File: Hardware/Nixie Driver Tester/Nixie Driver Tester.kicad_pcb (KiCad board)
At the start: 2 copper layers, 46.4 x 45.1 mm, 33 parts, among them J1 ICSP, J2 UJC-HP-3-SMT-TR, J3 OLED, Q1 MMBT2222A, Q2 MMBT2907ALT1G, Q3 FDD7N25LZTM, SW1 SW_Omron_B3FS

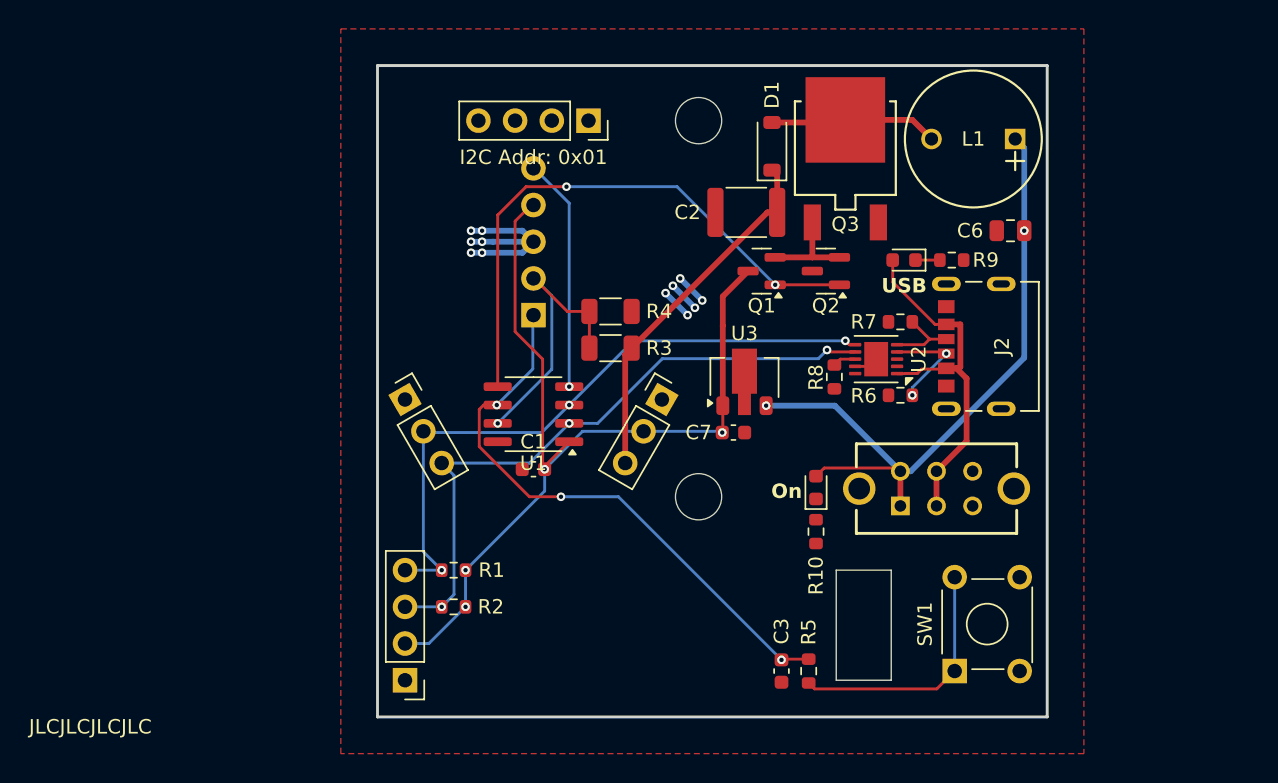
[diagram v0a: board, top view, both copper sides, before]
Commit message: Using a STM32 instead of a PIC
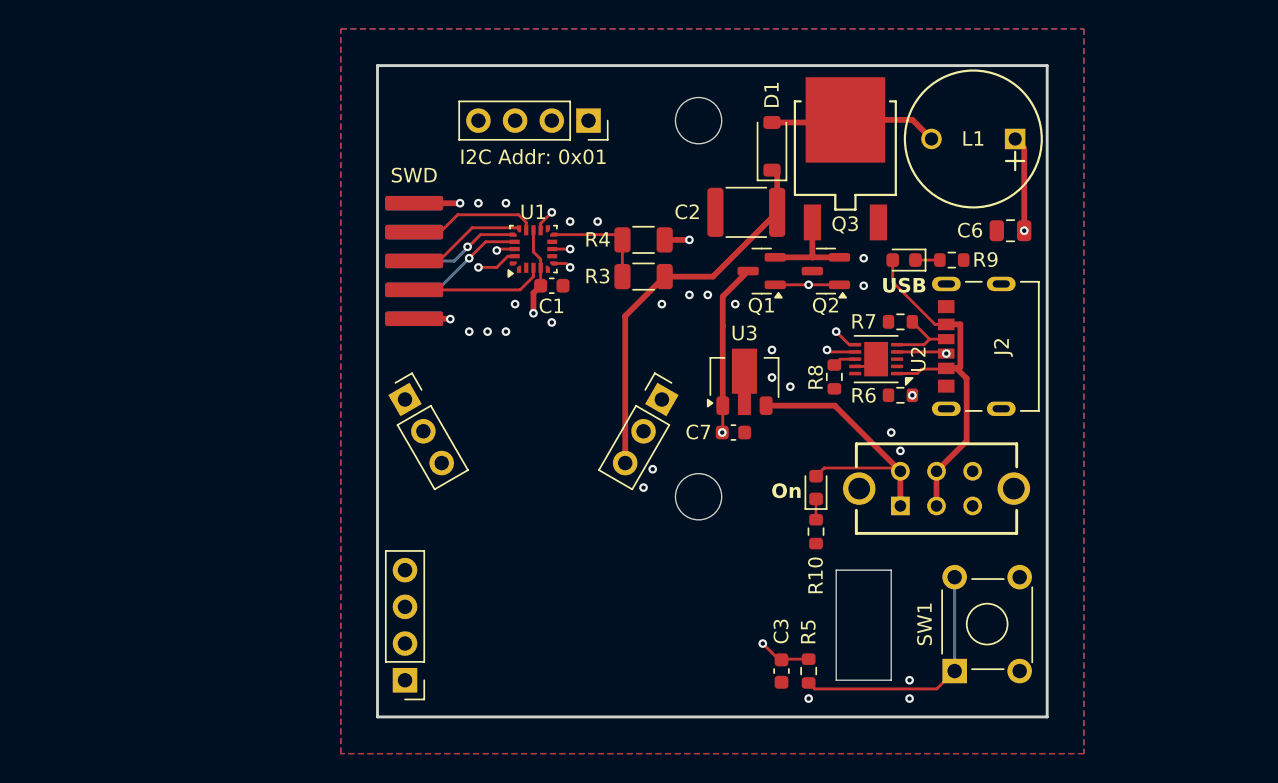
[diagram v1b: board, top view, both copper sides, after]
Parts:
- removed R1, R2: 5.1k, Resistor_SMD:R_0603_1608Metric
- J1: value ICSP -> SWD; footprint Connector_PinSocket_2.54mm:PinSocket_1x05_P2.54mm_Horizontal -> Connectory_PCB_Edge_:AVX-009159010061911
- U1: value ~ -> STM32L011F4Ux; footprint Package_SO:SOIC-8_3.9x4.9mm_P1.27mm -> Package_DFN_QFN:ST_UFQFPN-20_3x3mm_P0.5mm
- moved C1 12.8 mm to (135.9, 94.0)
- moved U1 11.4 mm to (134.6, 91.4), turned to 90 degrees
- moved J1 11.3 mm to (126.4, 88.3), turned to 90 degrees
- moved R3 5.46 mm to (142.2, 93.3)
- moved R4 5.46 mm to (142.2, 90.8)
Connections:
- C1 pad 1: /5V VRM/5V -> GND
- C1 pad 2: GND -> /5V VRM/5V
- J1 pad 1: /Button/Button -> unconnected-(J1-Pin_1-Pad1)
- J1 pad 2: /Controller/HVMON -> unconnected-(J1-Pin_2-Pad2)
- J1 pad 3: GND -> /Controller/SWDIO
- J1 pad 4: /5V VRM/5V -> /Controller/SWCLK
- J1 pad 5: Net-(J1-Pin_5) -> /Controller/SWO
- U1 pad 1: /5V VRM/5V -> unconnected-(U1-PC14-Pad1)
- U1 pad 2: /Controller/SCL -> unconnected-(U1-PC15-Pad2)
- U1 pad 3: /Controller/SDA -> /Controller/NRST
- U1 pad 4: Net-(J1-Pin_5) -> /5V VRM/5V
- U1 pad 5: /Boost Converter/PWM -> unconnected-(U1-PA0-Pad5)
- U1 pad 7: /Controller/HVMON -> unconnected-(U1-PA4-Pad7)
- U1 pad 8: GND -> /Boost Converter/PWM
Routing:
- net Net-(J1-Pin_5): track 16.2 -> 0.00 mm, vias 1 -> 0
- net /Boost Converter/PWM: track 39.2 -> 23.2 mm
- net GND: track 21.7 -> 8.43 mm, vias 12 -> 28
- net /Controller/HVMON: track 19.5 -> 7.37 mm, vias 1 -> 0
- net /Controller/SDA: track 45.3 -> 57.4 mm, vias 3 -> 2
- net /Controller/SCL: track 45.1 -> 56.3 mm, vias 3 -> 2
- net /Controller/NRST: track 0.00 -> 9.24 mm
- net /Controller/VCP_TX: track 0.00 -> 9.02 mm
- net /Controller/SWCLK: track 0.00 -> 8.33 mm, vias 0 -> 1
- net /Controller/VCP_RX: track 0.00 -> 8.21 mm
- net /Controller/SWDIO: track 0.00 -> 7.57 mm, vias 0 -> 1
- net /Button/Button: track 40.2 -> 36.4 mm, vias 3 -> 2
- net /5V VRM/VBUS: track 47.0 -> 49.8 mm, vias 2 -> 1
- net /Boost Converter/180V: track 25.2 -> 26.7 mm
- net /5V VRM/5V: track 64.7 -> 66.2 mm, vias 4 -> 3
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- added copper zone on B.Cu, net GND
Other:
- copper layers 2 -> 4
- board text removed: "JLCJLCJLCJLC"

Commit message: Swapped the power switch and USB-C port
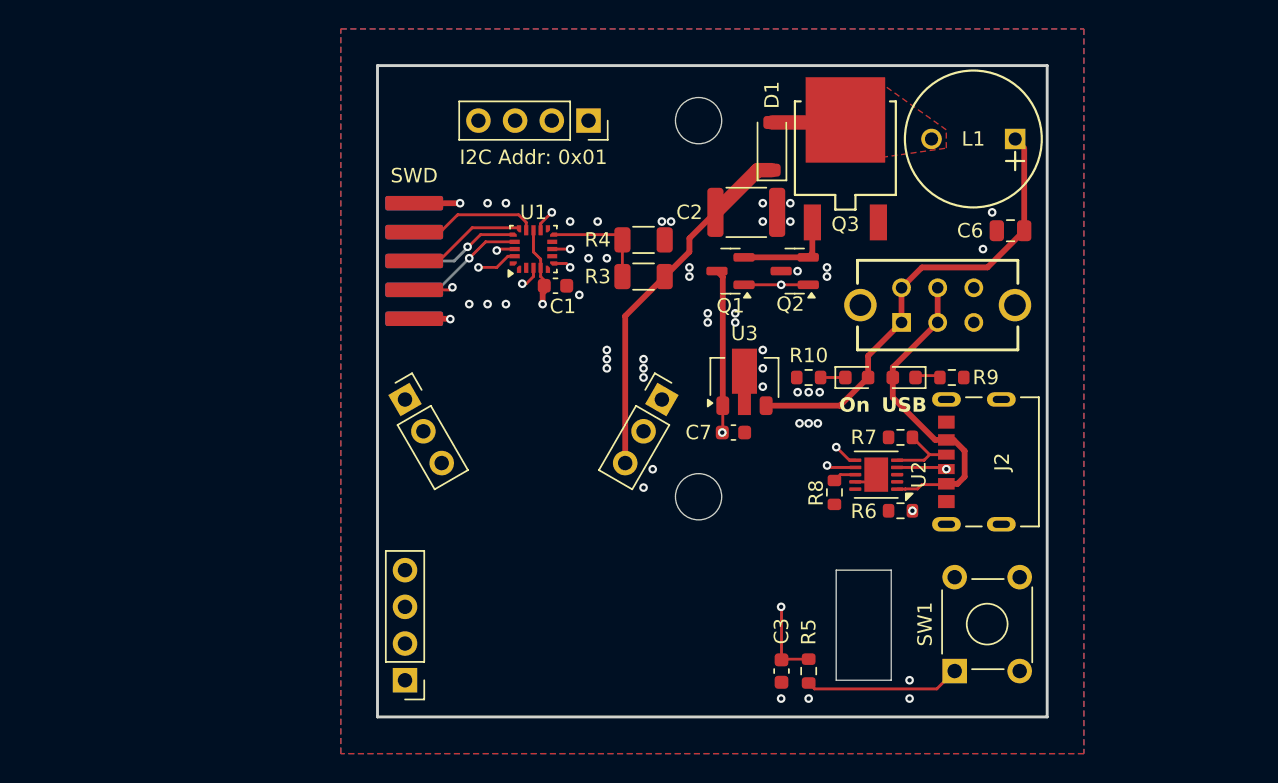
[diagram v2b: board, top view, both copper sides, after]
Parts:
- moved S1 12.7 mm to (160.1, 96.5)
- moved R10 10.7 mm to (153.7, 100.3), turned to 180 degrees
- moved D3 8.13 mm to (160.3, 100.3)
- moved R9 8.13 mm to (163.6, 100.3)
- moved D2 8.12 mm to (157.0, 100.3), turned to 0 degrees
- moved J2 8.00 mm to (163.2, 106.2)
- moved R6 8.00 mm to (160.0, 109.6)
- moved U2 8.00 mm to (158.3, 107.1)
- moved R7 8.00 mm to (160.0, 104.5)
- moved R8 8.00 mm to (155.5, 108.3)
- moved Q1 2.16 mm to (148.3, 93.0)
- moved Q2 2.16 mm to (152.7, 93.0)
- moved C1 0.25 mm to (136.1, 94.0)
- turned C2 to 0 degrees
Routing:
- net /5V VRM/VBUS: track 49.8 -> 31.8 mm, vias 1 -> 0
- net Net-(D1-A): track 11.7 -> 5.15 mm
- net /Controller/SCL: track 56.3 -> 62.3 mm
- net /Controller/SDA: track 57.4 -> 61.6 mm
- net /USB PD/VBUS In: track 25.6 -> 22.2 mm
- net /Boost Converter/PWM: track 23.2 -> 21.3 mm
- net GND: track 8.43 -> 6.72 mm, vias 28 -> 50
- net /Boost Converter/180V: track 26.7 -> 25.1 mm
- net /Controller/NRST: vias 0 -> 2
- added copper zone on F.Cu, net Net-(D1-A)
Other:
- board text added: "Nixie Driver Tester Aaron Johnson 09/20/2026"
- board text removed: "Nixie Driver Tester Aaron Johnson 02/09/2026"

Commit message: Switch mode 3.3V and SMD inductor
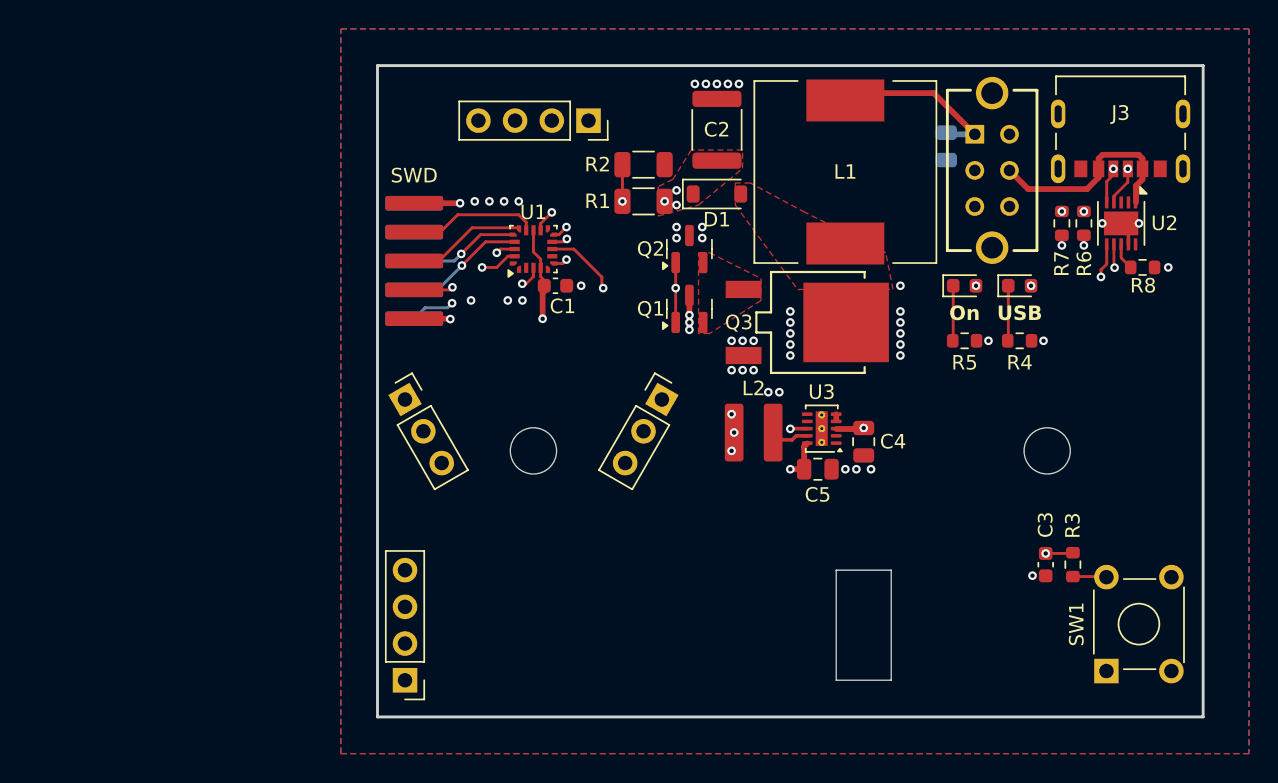
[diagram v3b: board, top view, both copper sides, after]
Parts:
- removed C7: 100nF, Capacitor_SMD:C_0603_1608Metric
- added C4: 2.2uF, Capacitor_SMD:C_0805_2012Metric, F.Cu at (157.5, 104.8)
- added C5: 22uF, Capacitor_SMD:C_0805_2012Metric, F.Cu at (154.3, 106.7)
- added L2: VLS4012CX-100M-1, Inductor_:TDK LPS40xx, F.Cu at (151.2, 104.1)
- C6: value 1uF -> 100nF; moved to B.Cu
- L1: footprint Inductor_:Bourns RLB1014 -> Inductor_SMD:L_Wuerth_WE-PD-Typ-LS
- U2: value ~ -> HUSB238
- U3: value ~ -> TPS62177DQC; footprint Package_TO_SOT_SMD:SOT-89-3 -> Package_SON:WSON-10-1EP_2x3mm_P0.5mm_EP0.84x2.4mm_ThermalVias
- moved H2 33.2 mm to (170.2, 105.4)
- moved R8 26.4 mm to (176.8, 92.7), turned to 0 degrees
- moved U2 24.3 mm to (175.3, 89.7), turned to -90 degrees
- moved R6 23.6 mm to (172.7, 89.7), turned to 90 degrees
- moved J3 23.6 mm to (175.3, 85.9), turned to 180 degrees
- moved C3 19.7 mm to (170.1, 113.3)
- moved R3 19.7 mm to (172.0, 113.3)
- moved R7 18.6 mm to (171.2, 89.7), turned to -90 degrees
- moved S1 14.0 mm to (165.2, 83.5), turned to -90 degrees
- moved Q3 12.2 mm to (154.3, 96.5), turned to -90 degrees
- moved L1 12.0 mm to (156.2, 86.1), turned to -90 degrees
- moved H1 11.9 mm to (134.6, 105.4)
- moved R5 11.1 mm to (164.5, 97.8), turned to 0 degrees
- moved SW1 10.5 mm to (174.3, 120.7)
- moved D2 10.2 mm to (168.3, 94.0), turned to 0 degrees
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- renumbered D3 to D2, D2 to D3, J3 to J1, J1 to J2, J2 to J3, R3 to R1, R4 to R2, R5 to R3, R9 to R4, R10 to R5
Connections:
- net Net-(D1-A) renamed /Boost Converter/Boost Src
- net Net-(D2-K) renamed /USB PD/PWR LED
- net Net-(D3-K) renamed /USB PD/USB LED
- net Net-(Q1-E) renamed /Boost Converter/Gate Drive
- C1 pad 2: /5V VRM/5V -> /VCC VRM/V_Out
- C6 pad 1: /5V VRM/VBUS -> GND
- C6 pad 2: GND -> /Boost Converter/VBUS
- D3 pad 2: /5V VRM/VBUS -> /Boost Converter/VBUS
- J1 pad 2: /5V VRM/5V -> /VCC VRM/V_Out
- J2 pad 10: /5V VRM/5V -> /VCC VRM/V_Out
- L1 pad 1: /5V VRM/VBUS -> /Boost Converter/VBUS
- N1 pad 9: /5V VRM/5V -> /VCC VRM/V_Out
- Q1 pad 3: /5V VRM/5V -> /VCC VRM/V_Out
- S1 pad 1: /5V VRM/VBUS -> /Boost Converter/VBUS
- S1 pad 6: /5V VRM/VBUS -> /Boost Converter/VBUS
- U1 pad 13: /5V VRM/5V -> /VCC VRM/V_Out
- U1 pad 4: /5V VRM/5V -> /VCC VRM/V_Out
- U1 pad 9: unconnected-(U1-PA6-Pad9) -> /Controller/SWO
- U3 pad 1: /5V VRM/5V -> GND
- U3 pad 2: GND -> /Boost Converter/VBUS
- U3 pad 3: /5V VRM/VBUS -> /Boost Converter/VBUS
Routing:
- net /VCC VRM/V_Out: track 0.00 -> 79.8 mm, vias 0 -> 10
- net /5V VRM/5V: track 66.2 -> 0.00 mm, vias 3 -> 0
- net /Boost Converter/VBUS: track 0.00 -> 41.2 mm, vias 0 -> 2
- net /5V VRM/VBUS: track 31.8 -> 0.00 mm
- net /Button/Button: track 36.3 -> 51.2 mm
- net /Controller/SWO: track 0.00 -> 14.7 mm, vias 0 -> 2
- net /Controller/SCL: track 62.3 -> 73.4 mm
- net /Controller/SDA: track 61.6 -> 72.4 mm
- net Net-(R3-Pad2): track 17.3 -> 8.84 mm
- net /Boost Converter/PWM: track 21.3 -> 14.3 mm
- net /Boost Converter/Gate Drive: track 6.98 -> 0.00 mm
- net /Boost Converter/Boost Src: track 5.15 -> 0.00 mm
- net /Boost Converter/180V: track 25.1 -> 21.3 mm, vias 0 -> 3
- net /USB PD/VBUS In: track 22.2 -> 25.8 mm, vias 0 -> 1
- net /VCC VRM/VRM SW: track 0.00 -> 2.69 mm
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- added copper zone on F.Cu, net /Boost Converter/180V
- added copper zone on F.Cu, net /Boost Converter/Gate Drive
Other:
- board size 46.4 x 45.1 mm -> 57.1 x 45.1 mm
- board text added: "Nixie Driver Tester Aaron Johnson 09/27/2026"
- board text removed: "Nixie Driver Tester Aaron Johnson 09/20/2026"

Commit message: Moved last back component to the board front
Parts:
- C6: moved to F.Cu
- moved C6 4.30 mm to (164.6, 80.3), turned to 180 degrees
- moved R4 3.14 mm to (170.4, 95.5), turned to 90 degrees
- moved R5 3.14 mm to (162.3, 95.5), turned to 90 degrees
- moved S1 2.14 mm to (165.2, 85.6)
- moved D2 1.57 mm to (168.7, 95.5), turned to 90 degrees
- moved D3 1.57 mm to (164.1, 95.5), turned to 90 degrees
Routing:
- net /Boost Converter/VBUS: track 41.2 -> 33.6 mm, vias 2 -> 4
- net /USB PD/USB LED: track 3.83 -> 1.79 mm
- net /USB PD/PWR LED: track 3.83 -> 1.79 mm
- net GND: track 6.61 -> 8.48 mm
- net /USB PD/VBUS In: track 25.8 -> 24.3 mm, vias 1 -> 0
- net /Controller/SCL: track 73.4 -> 73.9 mm
- net /VCC VRM/V_Out: track 79.8 -> 80.3 mm, vias 10 -> 11
- added copper zone on F.Cu, net /Boost Converter/VBUS

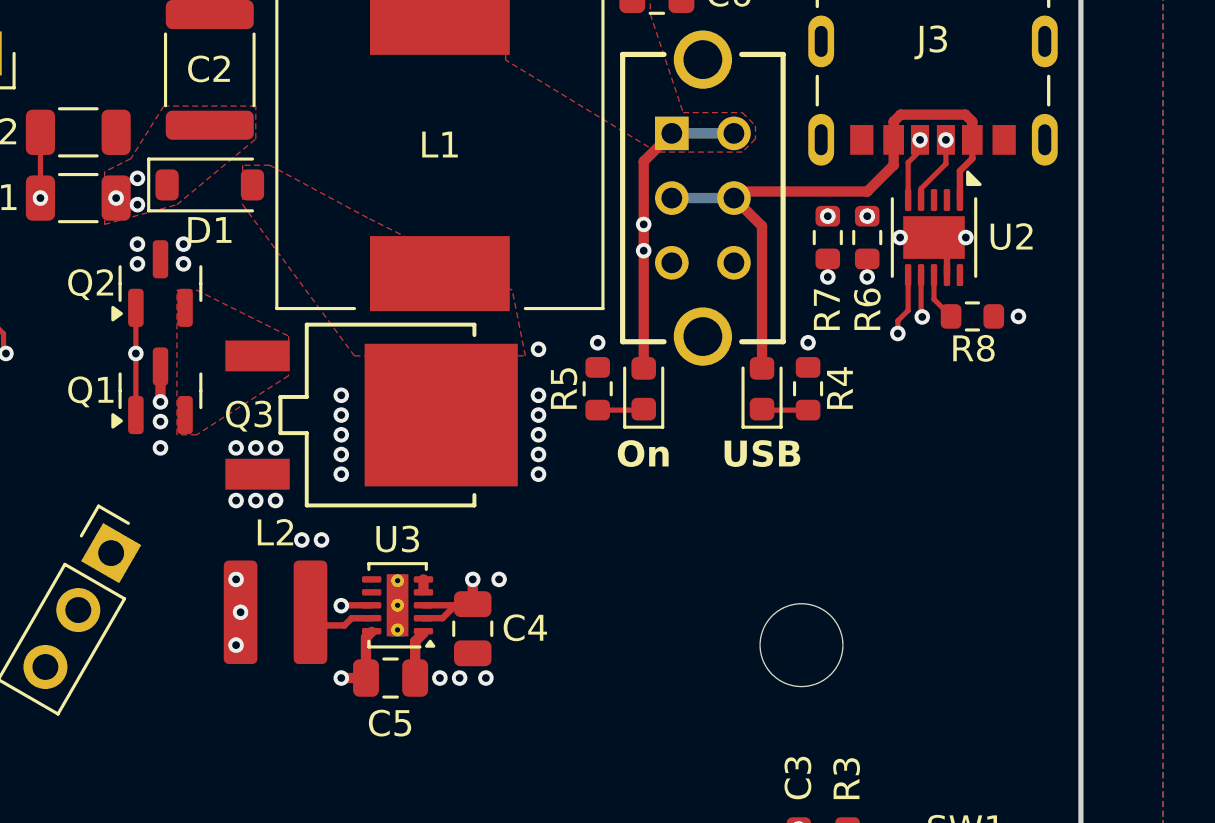
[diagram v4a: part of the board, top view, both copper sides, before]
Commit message: Moved USB LED
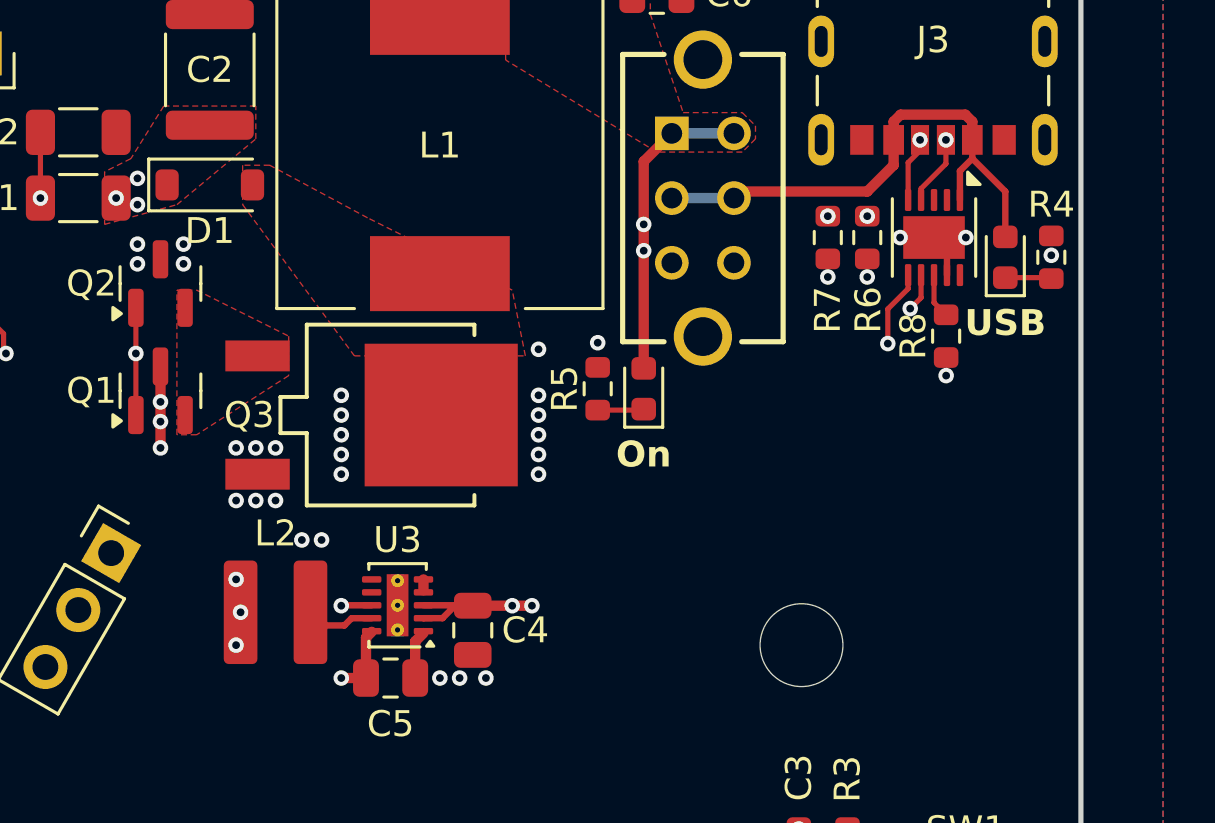
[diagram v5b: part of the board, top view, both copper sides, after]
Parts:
- moved D2 10.7 mm to (178.1, 90.4)
- moved R4 10.7 mm to (179.8, 90.4)
- moved R8 1.27 mm to (175.8, 93.5), turned to -90 degrees
- moved C4 0.06 mm to (157.5, 104.8)
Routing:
- net /USB PD/VBUS In: track 24.3 -> 20.8 mm
- net /Boost Converter/VBUS: track 33.6 -> 35.6 mm
- net /VCC VRM/V_Out: track 80.3 -> 82.0 mm
- net /Controller/SCL: track 73.9 -> 73.2 mm
